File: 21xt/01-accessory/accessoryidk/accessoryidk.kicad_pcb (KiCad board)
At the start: 2 copper layers, 118 x 79 mm, 81 parts, among them IC1 LT6658AHMSE-2.5#PBF, IC10 AD7175-8BCPZ-RL7, IC2 LT6658AHMSE-5#PBF, IC3 REF5025AIDR, IC5 INA821IDGKT, IC6 TXB0108PWR, IC7 REF5050IDR, IC8 INA821IDGKT, IC9 INA821IDGKT, J1 Conn_01x04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

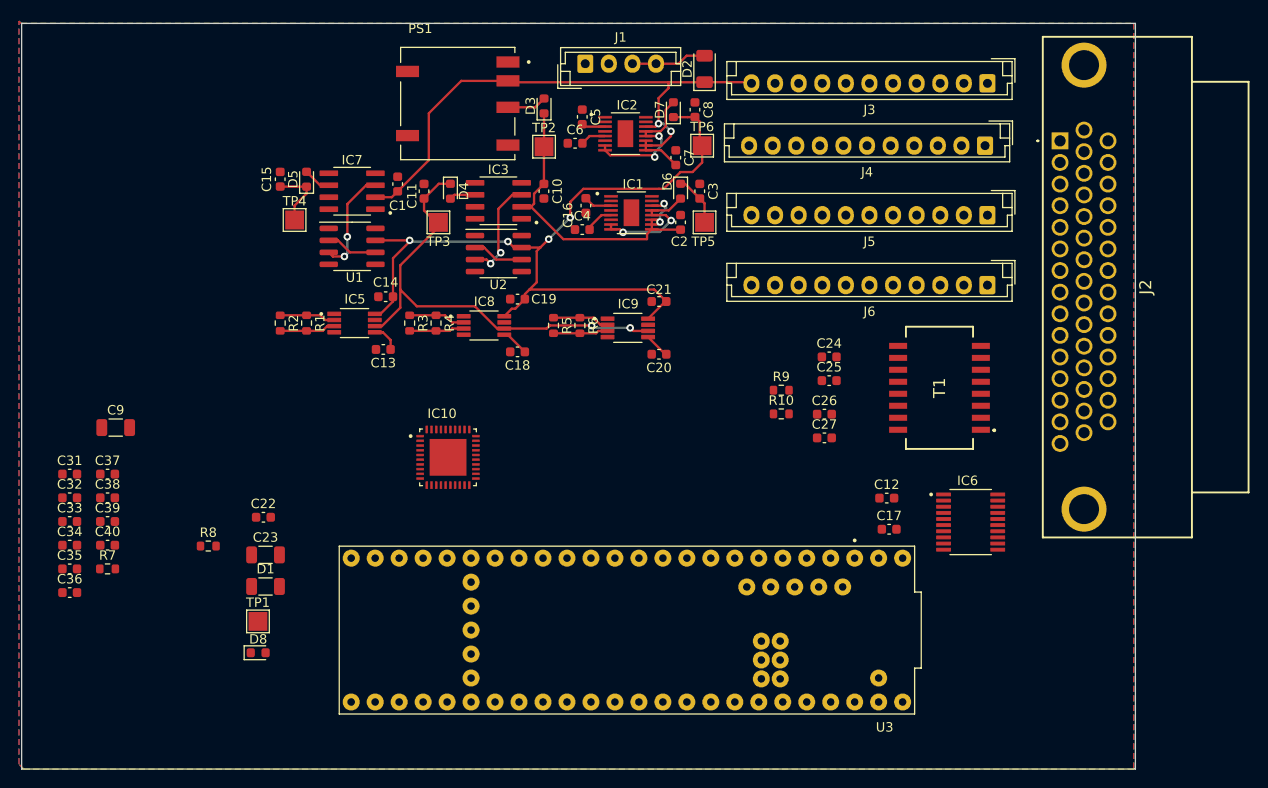
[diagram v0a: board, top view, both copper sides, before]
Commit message: Finished Accessory V1 schematic, need DRC checks
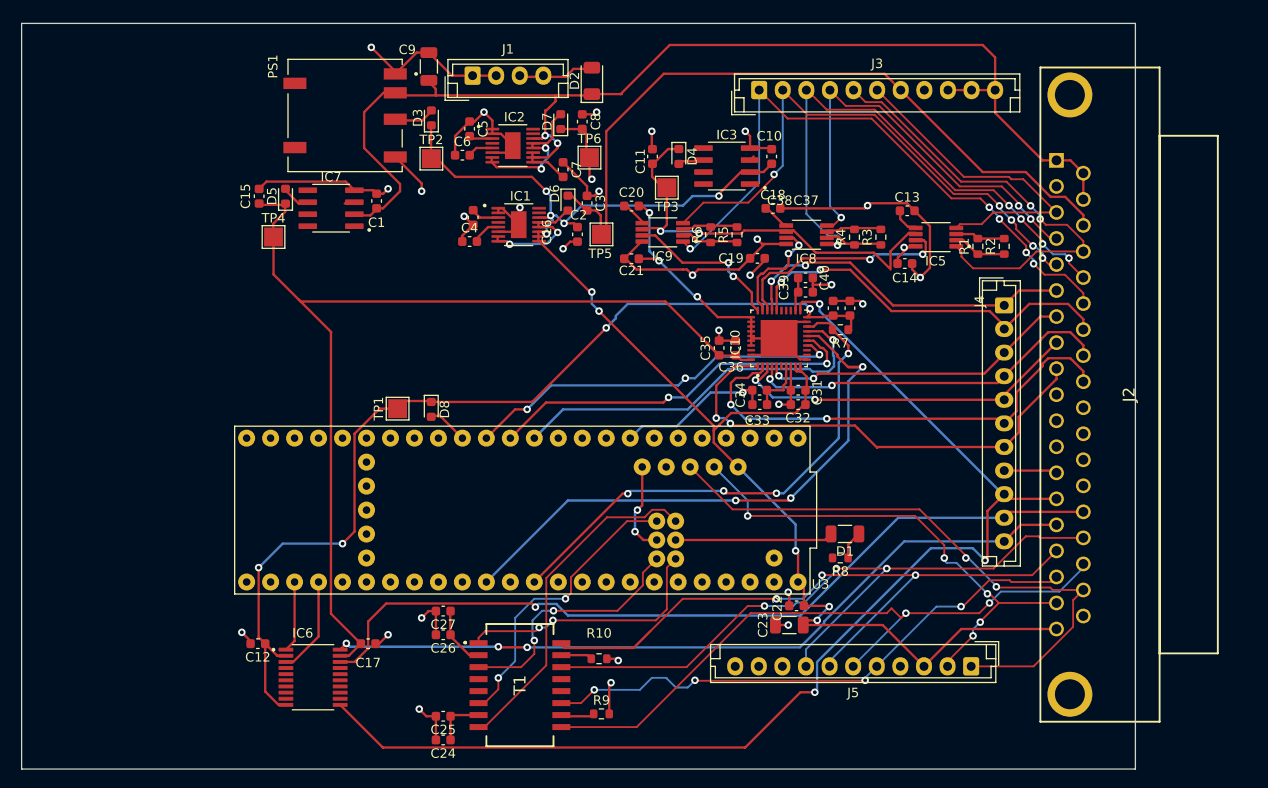
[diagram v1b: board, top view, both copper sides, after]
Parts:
- removed J6: Conn_01x11, Connector_JST:JST_EH_B11B-EH-A_1x11_P2.50mm_Vertical
- removed U1, U2: OPA333AIDBVR, Package_SO:SOIC-8_3.9x4.9mm_P1.27mm
- J2: value DB-44 Connector -> 5747847-6; footprint 21xt_footprints:23117702 -> 21xt_footprints:57478476
- moved R7 81.7 mm to (100.2, 46.2), turned to 180 degrees
- moved C38 81.2 mm to (101.3, 43.9), turned to 90 degrees
- moved C40 79.2 mm to (96.5, 40.7)
- moved C37 78.9 mm to (99.5, 43.9), turned to 90 degrees
- moved C39 77.8 mm to (96.5, 42.2)
- moved C32 77.8 mm to (95.8, 54.1), turned to 180 degrees
- moved C31 77.7 mm to (95.8, 52.6), turned to 180 degrees
- moved R2 77.1 mm to (117.6, 37.3), turned to 90 degrees
- moved C36 75.2 mm to (89.1, 48.1), turned to 90 degrees
- moved C34 74.9 mm to (91.7, 52.6)
- moved C33 74.1 mm to (91.7, 54.1)
- moved C35 72.7 mm to (87.4, 48.1), turned to 90 degrees
- moved IC6 71.6 mm to (44.4, 83.0)
- moved R1 71.6 mm to (114.8, 37.3), turned to 90 degrees
- moved C12 68.4 mm to (38.5, 79.4), turned to 180 degrees
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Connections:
- C12 pad 2: GNDD -> Earth
- IC10 pad 1: sg1 -> brakespeed2
- IC10 pad 11: GND -> usb_gnd
- IC10 pad 19: GND -> usb_gnd
- IC10 pad 2: sg2 -> brakespeed1
- IC10 pad 26: wheelspeed1 -> linpot2
- IC10 pad 27: wheelspeed2 -> linpot1
- IC10 pad 28: potentiometer -> sg1
- IC10 pad 29: brakespeed1 -> sg2
- IC10 pad 3: sg3 -> potentiometer
- IC10 pad 30: brakespeed2 -> sg3
- IC10 pad 31: GND -> usb_gnd
- IC10 pad 32: GND -> usb_gnd
- IC10 pad 33: GND -> usb_gnd
- IC10 pad 34: GND -> usb_gnd
- IC10 pad 35: GND -> usb_gnd
- IC10 pad 36: GND -> usb_gnd
- IC10 pad 37: GND -> usb_gnd
- IC10 pad 39: GND -> usb_gnd
- IC10 pad 4: linpot1 -> wheelspeed2
- IC10 pad 41: GND -> usb_gnd
- IC10 pad 5: linpot2 -> wheelspeed1
- IC3 pad 3: Net-(IC3-TEMP) -> unconnected-(IC3-TEMP-Pad3)
- IC6 pad 10: 3.3v -> 3V3
- IC7 pad 3: Net-(IC7-TEMP) -> unconnected-(IC7-TEMP-Pad3)
- J2 pad 10: brakespeed1 -> Earth
- J2 pad 11: hallfx2 -> Earth
- J2 pad 12: hallfx1 -> Earth
- J2 pad 13: Tx+ -> Earth
- J2 pad 14: usb_d+ -> GNDD
- J2 pad 15: usb_d- -> hallfx1
- J2 pad 16: 12v -> Rx+
- J2 pad 17: Earth -> Tx+
- J2 pad 18: Earth -> usb_d-
- J2 pad 19: sg1+ -> 5v_buck
- J2 pad 2: 2.5v -> 5v_reful
- J2 pad 20: sg2- -> 12v
- J2 pad 21: sg3- -> 12v
- J2 pad 22: linpot2 -> 2.5v
- J2 pad 23: Earth -> sg1-
- J2 pad 24: Earth -> sg2-
- J2 pad 25: Earth -> sg3-
- J2 pad 26: Earth -> linpot2
- J2 pad 27: Earth -> wheelspeed2
- J2 pad 28: Tx- -> brakespeed1
- J2 pad 29: Rx+ -> Earth
- J2 pad 3: 5v_reful -> sg1+
- J2 pad 30: 5v_buck -> Earth
- J2 pad 31: 12v -> Earth
- J2 pad 33: Earth -> hallfx2
- J2 pad 34: sg1- -> Rx-
- J2 pad 35: Earth -> Tx-
- J2 pad 36: Earth -> usb_d+
- J2 pad 37: wheelspeed2 -> usb_gnd
- J3 pad 1: unconnected-(J3-Pin_1-Pad1) -> sg3-
- J3 pad 10: 2.5v -> 12v
- J3 pad 2: unconnected-(J3-Pin_2-Pad2) -> sg3+
- J3 pad 3: unconnected-(J3-Pin_3-Pad3) -> sg2-
- J3 pad 4: unconnected-(J3-Pin_4-Pad4) -> sg2+
- J3 pad 5: unconnected-(J3-Pin_5-Pad5) -> sg1-
- J3 pad 6: unconnected-(J3-Pin_6-Pad6) -> sg1+
- J3 pad 7: sg2- -> 2.5v
- J3 pad 8: sg2+ -> 5v_reful
- J3 pad 9: 5v_reful -> 12v
- J4 pad 1: unconnected-(J4-Pin_1-Pad1) -> linpot1
- J4 pad 10: unconnected-(J4-Pin_10-Pad10) -> hallfx2
- J4 pad 11: unconnected-(J4-Pin_11-Pad11) -> hallfx1
- J4 pad 2: unconnected-(J4-Pin_2-Pad2) -> linpot2
- J4 pad 3: unconnected-(J4-Pin_3-Pad3) -> wheelspeed1
- J4 pad 4: unconnected-(J4-Pin_4-Pad4) -> wheelspeed2
- J4 pad 5: unconnected-(J4-Pin_5-Pad5) -> potentiometer
- J4 pad 6: unconnected-(J4-Pin_6-Pad6) -> brakespeed1
- J4 pad 7: unconnected-(J4-Pin_7-Pad7) -> brakespeed2
- J4 pad 8: unconnected-(J4-Pin_8-Pad8) -> Earth
- J4 pad 9: unconnected-(J4-Pin_9-Pad9) -> GNDD
- J5 pad 1: unconnected-(J5-Pin_1-Pad1) -> usb_d+
- J5 pad 2: unconnected-(J5-Pin_2-Pad2) -> usb_d-
- J5 pad 3: unconnected-(J5-Pin_3-Pad3) -> 5v_buck
- J5 pad 4: unconnected-(J5-Pin_4-Pad4) -> usb_gnd
- J5 pad 5: unconnected-(J5-Pin_5-Pad5) -> Tx+
- J5 pad 6: unconnected-(J5-Pin_6-Pad6) -> Tx-
- J5 pad 7: unconnected-(J5-Pin_7-Pad7) -> Rx+
- J5 pad 8: unconnected-(J5-Pin_8-Pad8) -> Rx-
- R8 pad 2: usb_gnd -> GNDA
- U3 pad 14: rst2 -> unconnected-(U3-A0-Pad14)
- U3 pad 16: v_temp1 -> unconnected-(U3-A2-Pad16)
- U3 pad 17: v_temp2 -> unconnected-(U3-A3-Pad17)
- U3 pad 18: hallfx1_3v3 -> unconnected-(U3-A4-Pad18)
- U3 pad 19: hallfx2_3v3 -> unconnected-(U3-A5-Pad19)
- U3 pad 2: 5v_buck -> unconnected-(U3-OUT2-Pad2)
- U3 pad 3: usb_d- -> unconnected-(U3-LRCLK2-Pad3)
- U3 pad 35: unconnected-(U3-TX8-Pad35) -> hallfx1_3v3
- U3 pad 36: unconnected-(U3-CS2-Pad36) -> hallfx2_3v3
- U3 pad 4: usb_d+ -> unconnected-(U3-BCLK2-Pad4)
- U3 pad 5V: unconnected-(U3-Pad5V) -> 5v_buck
- U3 pad D+: unconnected-(U3-PadD+) -> usb_d+
- U3 pad D-: unconnected-(U3-PadD-) -> usb_d-
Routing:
- net GNDD: track 0.00 -> 127.0 mm, vias 0 -> 3
- net 5v_buck: track 35.2 -> 157.8 mm, vias 2 -> 10
- net usb_gnd: track 0.00 -> 109.4 mm, vias 0 -> 14
- net 3V3: track 0.00 -> 104.9 mm, vias 0 -> 4
- net 5v_ref: track 6.86 -> 109.0 mm
- net Earth: track 0.00 -> 100.1 mm, vias 0 -> 18
- net hallfx2: track 0.00 -> 88.3 mm, vias 0 -> 1
- net hallfx1: track 0.00 -> 81.8 mm, vias 0 -> 3
- net Rx-: track 0.00 -> 75.1 mm, vias 0 -> 3
- net 2.5v: track 4.95 -> 77.4 mm
- net Tx-: track 0.00 -> 71.5 mm, vias 0 -> 2
- net Rx+: track 0.00 -> 70.6 mm, vias 0 -> 3
- net sg3-: track 0.00 -> 66.2 mm, vias 0 -> 5
- net 12v: track 63.3 -> 129.1 mm
- net usb_d+: track 0.00 -> 64.1 mm, vias 0 -> 2
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- added copper zone on In2.Cu, net 5v_reful
- added copper zone on In1.Cu, net Earth
- added copper zone on In2.Cu, net usb_gnd
- removed copper zone on B.Cu, net Earth
- removed copper zone on F.Cu, net Earth
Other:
- copper layers 2 -> 4

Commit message: Editing V1 accessory layout
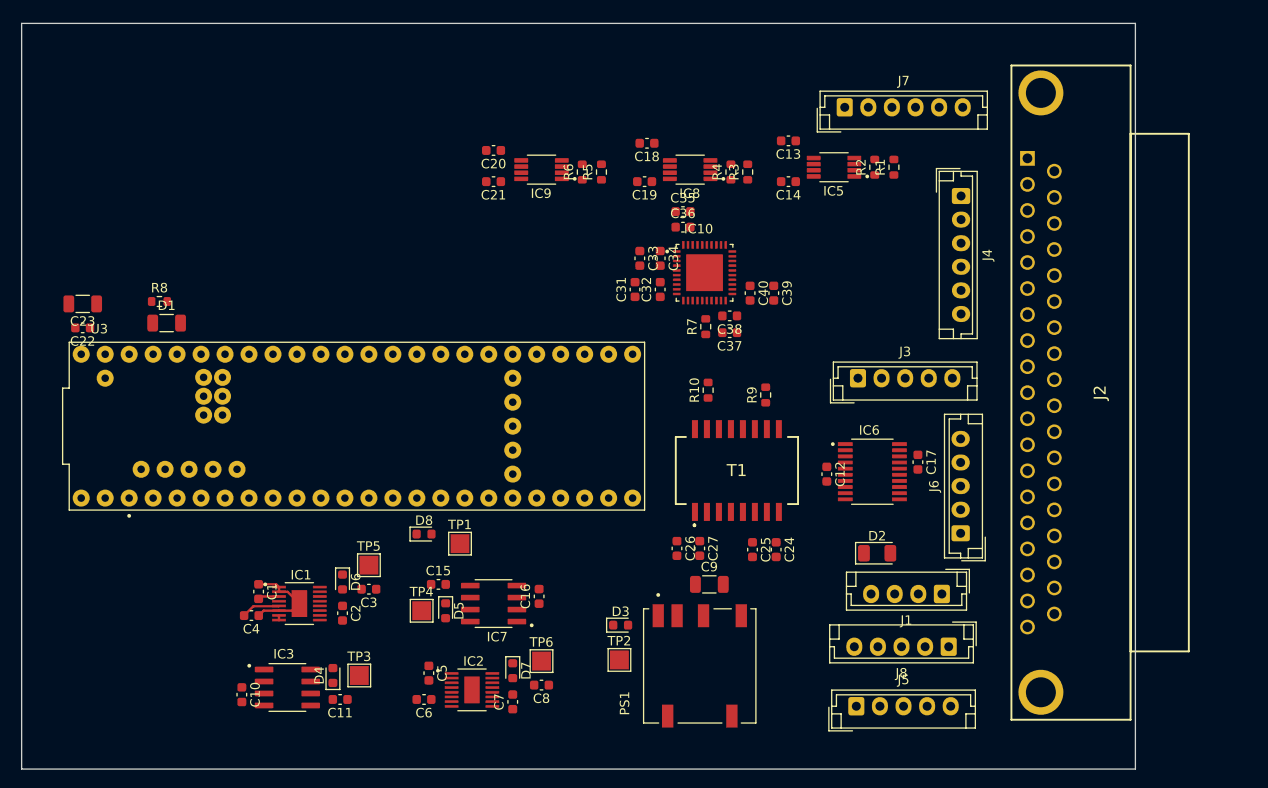
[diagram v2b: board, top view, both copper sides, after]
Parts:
- added J6: Conn_01x05, Connector_JST:JST_EH_B5B-EH-A_1x05_P2.50mm_Vertical, F.Cu at (113.0, 67.7)
- added J7: Conn_01x06, Connector_JST:JST_EH_B6B-EH-A_1x06_P2.50mm_Vertical, F.Cu at (100.7, 22.6)
- added J8: Conn_01x05, Connector_JST:JST_EH_B5B-EH-A_1x05_P2.50mm_Vertical, F.Cu at (111.7, 79.8)
- J3, J5: value Conn_01x11 -> Conn_01x05; footprint Connector_JST:JST_EH_B11B-EH-A_1x11_P2.50mm_Vertical -> Connector_JST:JST_EH_B5B-EH-A_1x05_P2.50mm_Vertical
- J4: value Conn_01x11 -> Conn_01x06; footprint Connector_JST:JST_EH_B11B-EH-A_1x11_P2.50mm_Vertical -> Connector_JST:JST_EH_B6B-EH-A_1x06_P2.50mm_Vertical
- R1, R4, R6: value 200 -> 249
- moved C23 82.2 mm to (20.0, 43.4), turned to 180 degrees
- moved C22 81.2 mm to (20.0, 46.0), turned to 180 degrees
- moved C10 80.0 mm to (36.8, 84.8), turned to -90 degrees
- moved R8 77.1 mm to (28.1, 43.2), turned to 0 degrees
- moved D1 75.3 mm to (28.9, 45.5), turned to 0 degrees
- moved J1 74.1 mm to (111.0, 74.2), turned to 180 degrees
- moved IC3 72.2 mm to (41.7, 84.1), turned to 0 degrees
- moved PS1 69.4 mm to (85.3, 81.8), turned to 90 degrees
- moved C11 66.4 mm to (47.2, 85.3), turned to 180 degrees
- moved D4 66.1 mm to (46.5, 82.8), turned to 90 degrees
- moved IC6 63.1 mm to (103.6, 61.2)
- moved C12 62.9 mm to (98.8, 61.5), turned to -90 degrees
- moved C9 62.4 mm to (86.4, 73.2), turned to 0 degrees
- moved C17 61.3 mm to (108.5, 60.2), turned to -90 degrees
- moved TP3 61.1 mm to (49.3, 82.8), turned to 0 degrees
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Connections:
- C1 pad 1: Earth -> usb_gnd
- C10 pad 2: Earth -> usb_gnd
- C11 pad 2: Earth -> usb_gnd
- C12 pad 2: Earth -> usb_gnd
- C15 pad 2: Earth -> usb_gnd
- C16 pad 2: Earth -> usb_gnd
- C17 pad 2: Earth -> usb_gnd
- C2 pad 1: Earth -> usb_gnd
- C22 pad 1: Earth -> usb_gnd
- C23 pad 1: Earth -> usb_gnd
- C3 pad 1: Earth -> usb_gnd
- C31 pad 2: Earth -> usb_gnd
- C32 pad 2: Earth -> usb_gnd
- C35 pad 2: Earth -> usb_gnd
- C36 pad 2: Earth -> usb_gnd
- C37 pad 2: Earth -> usb_gnd
- C38 pad 2: Earth -> usb_gnd
- C4 pad 1: Earth -> usb_gnd
- C5 pad 1: Earth -> usb_gnd
- C6 pad 1: Earth -> usb_gnd
- C7 pad 1: Earth -> usb_gnd
- C8 pad 1: Earth -> usb_gnd
- C9 pad 2: Earth -> usb_gnd
- IC1 pad 1: Earth -> usb_gnd
- IC1 pad 17: Earth -> usb_gnd
- IC1 pad 2: Earth -> usb_gnd
- IC1 pad 6: Earth -> usb_gnd
- IC10 pad 1: brakespeed2 -> unconnected-(IC10-AIN16-Pad1)
- IC10 pad 2: brakespeed1 -> unconnected-(IC10-AIN0/REF2--Pad2)
- IC10 pad 21: GNDD -> usb_gnd
- IC10 pad 26: linpot2 -> unconnected-(IC10-AIN4-Pad26)
- IC10 pad 27: linpot1 -> unconnected-(IC10-AIN5-Pad27)
- IC10 pad 28: sg1 -> brakespeed2
- IC10 pad 29: sg2 -> brakespeed1
- IC10 pad 3: potentiometer -> unconnected-(IC10-AIN1/REF2+-Pad3)
- IC10 pad 30: sg3 -> potentiometer
- IC10 pad 31: usb_gnd -> wheelspeed2
- IC10 pad 32: usb_gnd -> wheelspeed1
- IC10 pad 33: usb_gnd -> linpot2
- IC10 pad 34: usb_gnd -> linpot1
- IC10 pad 35: usb_gnd -> sg1
- IC10 pad 36: usb_gnd -> sg2
- IC10 pad 37: usb_gnd -> sg3
- IC10 pad 4: wheelspeed2 -> unconnected-(IC10-AIN2-Pad4)
- IC10 pad 5: wheelspeed1 -> unconnected-(IC10-AIN3-Pad5)
- IC10 pad 8: Earth -> usb_gnd
- IC2 pad 1: Earth -> usb_gnd
- IC2 pad 17: Earth -> usb_gnd
- IC2 pad 2: Earth -> usb_gnd
- IC2 pad 6: Earth -> usb_gnd
- IC3 pad 4: Earth -> usb_gnd
- IC6 pad 11: GNDD -> usb_gnd
- IC7 pad 4: Earth -> usb_gnd
- J1 pad 1: Earth -> usb_gnd
- J1 pad 2: Earth -> usb_gnd
- J2 pad 1: 12v -> sg1+
- J2 pad 10: Earth -> usb_gnd
- J2 pad 11: Earth -> usb_gnd
- J2 pad 12: Earth -> hallfx1
- J2 pad 13: Earth -> 12v
- J2 pad 14: GNDD -> 12v
- J2 pad 15: hallfx1 -> 5v_reful
- J2 pad 16: Rx+ -> usb_d-
- J2 pad 17: Tx+ -> 5v_buck
- J2 pad 18: usb_d- -> Rx+
- J2 pad 19: 5v_buck -> Tx+
- J2 pad 2: 5v_reful -> sg2+
- J2 pad 20: 12v -> sg1-
- J2 pad 21: 12v -> sg2-
- J2 pad 22: 2.5v -> sg3-
- J2 pad 23: sg1- -> linpot2
- J2 pad 24: sg2- -> wheelspeed2
- J2 pad 25: sg3- -> brakespeed1
- J2 pad 26: linpot2 -> usb_gnd
- J2 pad 27: wheelspeed2 -> usb_gnd
- J2 pad 28: brakespeed1 -> usb_gnd
- J2 pad 29: Earth -> usb_gnd
- J2 pad 3: sg1+ -> sg3+
- J2 pad 30: Earth -> usb_gnd
- J2 pad 31: Earth -> hallfx2
- J2 pad 32: Earth -> 12v
- J2 pad 33: hallfx2 -> 2.5v
- J2 pad 34: Rx- -> usb_d+
- J2 pad 35: Tx- -> usb_gnd
- J2 pad 36: usb_d+ -> Rx-
- J2 pad 37: usb_gnd -> Tx-
- J2 pad 4: sg2+ -> linpot1
- J2 pad 5: sg3+ -> wheelspeed1
- J2 pad 6: linpot1 -> potentiometer
- J2 pad 7: wheelspeed1 -> brakespeed2
- J2 pad 8: potentiometer -> usb_gnd
- J2 pad 9: brakespeed2 -> usb_gnd
- J2 pad MH1: Earth -> usb_gnd
- J2 pad MH2: Earth -> usb_gnd
- J3 pad 1: sg3- -> brakespeed2
- J3 pad 2: sg3+ -> usb_gnd
- J3 pad 3: sg2- -> usb_gnd
- J3 pad 4: sg2+ -> hallfx2
- J3 pad 5: sg1- -> hallfx1
- J5 pad 1: usb_d+ -> Rx+
- J5 pad 2: usb_d- -> Rx-
- J5 pad 3: 5v_buck -> Tx+
- J5 pad 4: usb_gnd -> Tx-
- J5 pad 5: Tx+ -> unconnected-(J5-Pin_5-Pad5)
- PS1 pad 1: Earth -> usb_gnd
- PS1 pad 5: Earth -> usb_gnd
- R8 pad 2: GNDA -> usb_gnd
- U3 pad 5V: 5v_buck -> unconnected-(U3-Pad5V)
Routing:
- net 5v_buck: track 157.8 -> 0.00 mm, vias 10 -> 0
- net 12v: track 129.1 -> 0.00 mm, vias 2 -> 0
- net GNDD: track 127.0 -> 0.00 mm, vias 3 -> 0
- net 5v_ref: track 109.0 -> 0.00 mm
- net 3V3: track 104.9 -> 0.00 mm, vias 4 -> 0
- net Earth: track 100.1 -> 0.00 mm, vias 18 -> 0
- net usb_gnd: track 109.4 -> 10.3 mm, vias 14 -> 0
- net hallfx2: track 88.3 -> 0.00 mm, vias 1 -> 0
- net hallfx1: track 81.8 -> 0.00 mm, vias 3 -> 0
- net 2.5v: track 77.4 -> 0.00 mm
- net Rx-: track 75.1 -> 0.00 mm, vias 3 -> 0
- net Tx-: track 71.5 -> 0.00 mm, vias 2 -> 0
- net Rx+: track 70.6 -> 0.00 mm, vias 3 -> 0
- net sg3-: track 66.2 -> 0.00 mm, vias 5 -> 0
- net usb_d+: track 64.1 -> 0.00 mm, vias 2 -> 0
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- added copper zone on In1.Cu, net usb_gnd
- removed copper zone on In2.Cu, net 5v_reful
- removed copper zone on In1.Cu, net Earth
- removed copper zone on In2.Cu, net usb_gnd

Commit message: FINISHED accessory edited v1 layout, need to check silkscreen
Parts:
- moved C23 62.6 mm to (77.1, 69.2), turned to 0 degrees
- moved C22 60.7 mm to (77.1, 66.7), turned to 0 degrees
- moved D7 60.6 mm to (103.5, 35.0)
- moved IC2 60.6 mm to (99.2, 37.1)
- moved TP6 60.6 mm to (106.6, 34.0)
- moved C5 60.6 mm to (94.6, 35.3)
- moved C6 60.6 mm to (94.1, 38.1)
- moved C7 60.6 mm to (103.5, 38.4)
- moved C8 60.6 mm to (106.6, 36.6)
- moved C4 58.0 mm to (94.5, 88.9), turned to -90 degrees
- moved C1 55.2 mm to (91.9, 88.1), turned to 0 degrees
- moved IC1 51.0 mm to (93.2, 83.8), turned to 90 degrees
- moved C15 50.9 mm to (98.2, 42.3)
- moved C16 50.9 mm to (108.8, 43.6)
- moved D5 50.9 mm to (98.9, 45.1)
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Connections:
- J2 pad 15: 5v_reful -> usb_gnd
- J2 pad 8: usb_gnd -> 5v_reful
- J3 pad 3: usb_gnd -> 5v_reful
- J3 pad 4: hallfx2 -> hallfx1
- J3 pad 5: hallfx1 -> hallfx2
- J6 pad 1: 2.5v -> usb_gnd
- J6 pad 2: 5v_reful -> 2.5v
- J7 pad 1: sg3- -> sg3+
- J7 pad 2: sg3+ -> sg3-
- J7 pad 3: sg2- -> sg2+
- J7 pad 4: sg2+ -> sg2-
- J7 pad 5: sg1- -> sg1+
- J7 pad 6: sg1+ -> sg1-
- J8 pad 1: usb_d+ -> 5v_buck
- J8 pad 2: usb_d- -> usb_d+
- J8 pad 3: 5v_buck -> usb_d-
- U3 pad 16: unconnected-(U3-A2-Pad16) -> hallfx2_3v3
- U3 pad 17: unconnected-(U3-A3-Pad17) -> hallfx1_3v3
- U3 pad 35: hallfx1_3v3 -> unconnected-(U3-TX8-Pad35)
- U3 pad 36: hallfx2_3v3 -> unconnected-(U3-CS2-Pad36)
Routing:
- net usb_gnd: track 10.3 -> 179.2 mm, vias 0 -> 16
- net 5v_reful: track 0.00 -> 84.8 mm, vias 0 -> 3
- net 3V3: track 0.00 -> 77.9 mm
- net usb_d+: track 0.00 -> 77.1 mm, vias 0 -> 4
- net 12v: track 0.00 -> 71.3 mm, vias 0 -> 2
- net usb_d-: track 0.00 -> 70.8 mm, vias 0 -> 2
- net sg3-: track 0.00 -> 65.7 mm, vias 0 -> 1
- net Rx+: track 0.00 -> 62.9 mm, vias 0 -> 1
- net Rx-: track 0.00 -> 62.8 mm, vias 0 -> 3
- net hallfx2_3v3: track 0.00 -> 58.0 mm, vias 0 -> 1
- net Tx-: track 0.00 -> 57.5 mm, vias 0 -> 1
- net sg3+: track 0.00 -> 56.7 mm
- net 2.5v_ref: track 0.00 -> 55.3 mm, vias 0 -> 6
- net Tx+: track 0.00 -> 53.6 mm, vias 0 -> 1
- net hallfx1_3v3: track 0.00 -> 52.8 mm, vias 0 -> 1
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- added copper zone on In2.Cu, net 12v
- added copper zone on In2.Cu, net 5v_buck

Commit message: Finished accessory v1 layout and silkscreen
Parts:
- moved C9 1.30 mm to (78.6, 73.6)
- moved D3 1.30 mm to (69.2, 78.0)
- moved PS1 1.30 mm to (77.6, 82.3)
- moved TP2 1.30 mm to (69.1, 81.6)
- moved D7 0.38 mm to (103.9, 35.0)
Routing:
- net usb_gnd: track 179.2 -> 184.7 mm
- net Net-(D5-A): track 0.00 -> 3.84 mm
- net 12v: track 71.3 -> 73.5 mm, vias 2 -> 4
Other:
- board text added: "BJR @JHU 21xt Accessory V1"

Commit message: Edited accesory V1 ref names
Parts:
- C31, C35, C38: value 10uF -> 10u
- C32, C34, C36, C37, C39: value 0.1uF -> 0.1u
- C33, C40: value 1uF -> 1u
- C4, C6: value 0.1 -> 0.1u
- D1: footprint Capacitor_SMD:C_1206_3216Metric -> Diode_SMD:D_0603_1608Metric
- renumbered IC9 to IC4, IC10 to IC9, U3 to U1
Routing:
- net Net-(D1-K): track 2.33 -> 3.02 mm
- net Net-(D1-A): track 8.77 -> 9.45 mm

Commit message: Re-oriented teensy and added bom
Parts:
- moved D8 18.0 mm to (59.7, 45.5)
- moved TP1 18.0 mm to (63.0, 45.2)
- turned U1 to 90 degrees
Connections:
- U1 pad 16: hallfx2_3v3 -> hallfx1_3v3
- U1 pad 17: hallfx1_3v3 -> hallfx2_3v3
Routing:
- net Rd+: track 23.2 -> 51.4 mm, vias 3 -> 4
- net Td+: track 26.1 -> 47.8 mm, vias 1 -> 2
- net Rd-: track 33.1 -> 51.0 mm
- net Net-(D1-A): track 9.45 -> 27.1 mm, vias 0 -> 1
- net 12v: track 73.5 -> 56.9 mm
- net hallfx1_3v3: track 52.8 -> 68.3 mm
- net 3V3: track 77.9 -> 62.8 mm, vias 0 -> 2
- net Td-: track 26.3 -> 41.2 mm
- net SDI: track 41.9 -> 54.6 mm, vias 1 -> 2
- net hallfx2_3v3: track 58.0 -> 69.9 mm
- net !CS: track 40.9 -> 50.0 mm
- net !ERROR: track 47.7 -> 55.0 mm
- net usb_d+: track 77.1 -> 82.7 mm, vias 4 -> 1
- net usb_gnd: track 184.7 -> 190.0 mm
- net usb_d-: track 70.8 -> 75.7 mm, vias 2 -> 0
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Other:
- board size 118 x 79 mm -> 96.5 x 79 mm
